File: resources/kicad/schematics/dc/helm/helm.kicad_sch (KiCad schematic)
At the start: 222 parts, among them J1 19, J10 07, J11 04, J12 05, J13 06, J14 07, J146 02, J147 09, J148 03, J15 03, J151 03, J152 04, J155 11, J158 14, J159 18, J16 08, J160 20, J161 12, J162 24, J164 40, J165 11, J166 30, J167 14, J17 10, J170 37, J171 35, J172 36, J174 22, J175 16, J176 17, J177 04, J178 24, J179 13, J18 09, J181 42, J182 43, J183 41, J187 01, J188 10, J189 34, J19 05, J190 39, J191 32, J192 02, J194 11, J195 03, J196 38, J197 29, J198 31, J2 48, J20 07, J200 04, J201 15, J202 05, J203 06, J204 32, J205 08, J206 33, J207 09, J208 23, J209 23, J21 01, J210 27, J211 09, J212 22, J213 08, J214 28, J216 25, J217 26, J218 15, J219 21, J22 11, J220 16, J221 02, J223 17, J224 18, J225 06, J226 28, J228 12, J23 12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

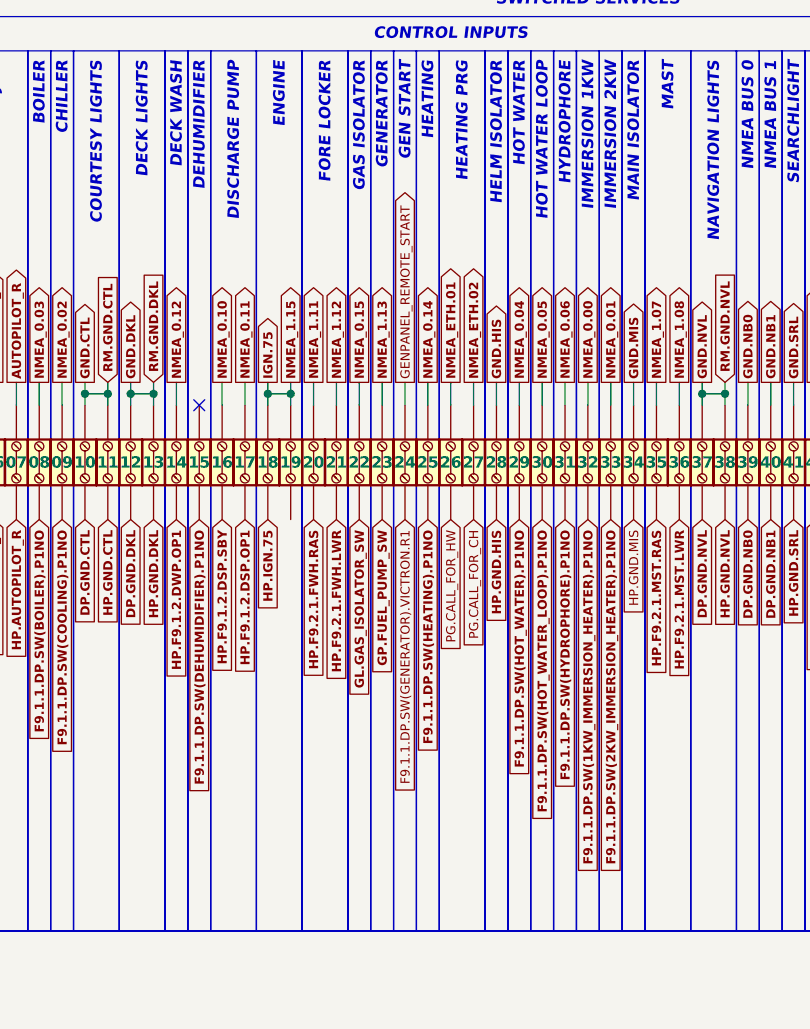
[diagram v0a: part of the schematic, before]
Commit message: Swap dimmer polarity
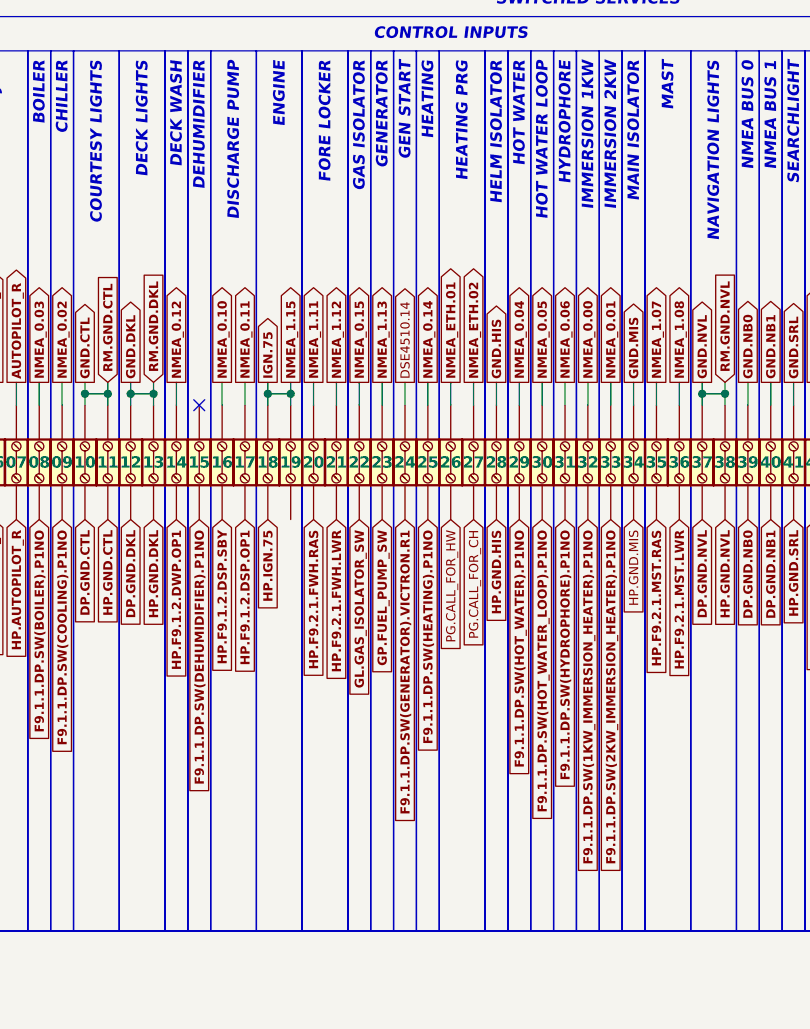
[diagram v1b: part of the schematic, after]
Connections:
- net GENPANEL_REMOTE_START is gone; now on net F9.1.1.DP.SW(GENERATOR).VICTRON.R1: J162. (Pin_2)
- new net: J261. (Pin_2), J262. (Pin_2)
- new net: J266. (Pin_2), J269. (Pin_2)
- new net DSE4510.14: J162. (Pin_2)
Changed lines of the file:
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@@
 		)
 	)
-	(global_label "GENPANEL_REMOTE_START"
+	(global_label "DSE4510.14"
 		(shape output)
 		(at 264.16 339.09 90)
@@
 			(font
 				(size 1.016 1.016)
-			)
-			(justify right)
+				(thickness 0.2032)
+				(bold yes)
+			)
+			(justify right)
